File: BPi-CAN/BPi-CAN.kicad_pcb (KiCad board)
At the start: 2 copper layers, 100 x 100 mm, 124 parts, among them J1 RJ45, J2 RJ45, J3 RJ45, J4 RJ45, P1 BPi, P10 SPI, P11 SNIFFER, P12 CAN-Bus, P13 USB, P14 CAN-Bus, P15 POWER, P16 CAN, P17 CAN, P18 CAN, P19 TERM, P2 S88, P20 S88 CONN, P21 RS232 Con, P22 S88, P23 CONN_01X08, P24 CONN_01X03, P25 I2C-Bus, P26 CONN_01X02, P3 CONN_02X04, P4 BPi Con, P5 TERM, P6 S88, P7 I2C-Bus, P8 RS485, P9 RS232, U1 MCP2562, U10 MCP2562, U11 6N137, U12 ISO1050, U13 FT230XS, U2 LM7805, U3 6N137, U4 6N137, U5 6N137, U6 6N137, U7 ADuM1251BR, U8 MAX3072E, U9 MAX3232

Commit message: wip
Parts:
- added P27: POWER, Pin_Headers:Pin_Header_Straight_1x02, F.Cu at (147.4, 124.0)
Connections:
- P14 pad 3: /CB6 -> /CB6'
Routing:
- net /CB6: track 57.2 -> 48.9 mm, vias 5 -> 4
- net /CB6': track 0.00 -> 6.09 mm
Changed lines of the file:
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@@
-(kicad_pcb (version 4) (host pcbnew 4.0.1-stable)
+(kicad_pcb (version 4) (host pcbnew 4.0.2+dfsg1-stable)
   (general
-    (links 284)
+    (links 285)
     (no_connects 0)
-    (area 99.924999 39.924999 200.075001 140.075001)
+    (area 86.872087 28.15 207.5 148.200001)
     (thickness 1.6)
     (drawings 107)
     (tracks 1798)
     (zones 0)
-    (modules 124)
-    (nets 133)
+    (modules 125)
+    (nets 134)
   )
   (page A4)
@@
   (net 131 "Net-(P1-Pad2)")
   (net 132 "Net-(P1-Pad4)")
+  (net 133 /CB6')
   (net_class Default "This is the default net class."
     (clearance 0.2)
@@
     (uvia_drill 0.1)
     (add_net /CB6)
+    (add_net /CB6')
     (add_net "Net-(P15-Pad2)")
     (add_net "Net-(P23-Pad1)")
@@
       (effects (font (size 1.5 1.5) (thickness 0.3)))
     )
-    (fp_text value CAN-Bus (at 4.1402 -8.9662 90) (layer F.SilkS)
+    (fp_text value CAN-Bus (at 6.883 -9.341 90) (layer F.SilkS)
       (effects (font (size 1.5 1.5) (thickness 0.3)))
     )
@@
       (net 56 /CVCC))
     (pad 3 thru_hole circle (at 0 -0.7 90) (size 2.4 2.4) (drill 1.2) (layers *.Cu *.Mask F.SilkS)
-      (net 53 /CB6))
+      (net 133 /CB6'))
     (pad 4 thru_hole circle (at -3.5 -0.7 90) (size 2.4 2.4) (drill 1.2) (layers *.Cu *.Mask F.SilkS)
       (net 54 /CB7))
@@
     )
   )
+  (module Pin_Headers:Pin_Header_Straight_1x02 (layer F.Cu)
+    (at 147.4 124 90)
+    (descr "Through hole pin header")
+    (tags "pin header")
+    (fp_text reference P27 (at 0 -5.1 90) (layer F.SilkS)
+      (effects (font (size 1 1) (thickness 0.15)))
+    )
+    (fp_text value POWER (at 0 -3.1 90) (layer F.Fab)
+      (effects (font (size 1 1) (thickness 0.15)))
+    )
+    (fp_line (start 1.27 1.27) (end 1.27 3.81) (layer F.SilkS) (width 0.15))
+    (fp_line (start 1.55 -1.55) (end 1.55 0) (layer F.SilkS) (width 0.15))
+    (fp_line (start -1.75 -1.75) (end -1.75 4.3) (layer F.CrtYd) (width 0.05))
+    (fp_line (start 1.75 -1.75) (end 1.75 4.3) (layer F.CrtYd) (width 0.05))
+    (fp_line (start -1.75 -1.75) (end 1.75 -1.75) (layer F.CrtYd) (width 0.05))
+    (fp_line (start -1.75 4.3) (end 1.75 4.3) (layer F.CrtYd) (width 0.05))
+    (fp_line (start 1.27 1.27) (end -1.27 1.27) (layer F.SilkS) (width 0.15))
+    (fp_line (start -1.55 0) (end -1.55 -1.55) (layer F.SilkS) (width 0.15))
+    (fp_line (start -1.55 -1.55) (end 1.55 -1.55) (layer F.SilkS) (width 0.15))
+    (fp_line (start -1.27 1.27) (end -1.27 3.81) (layer F.SilkS) (width 0.15))
+    (fp_line (start -1.27 3.81) (end 1.27 3.81) (layer F.SilkS) (width 0.15))
+    (pad 1 thru_hole rect (at 0 0 90) (size 2.032 2.032) (drill 1.016) (layers *.Cu *.Mask F.SilkS)
+      (net 53 /CB6))
+    (pad 2 thru_hole oval (at 0 2.54 90) (size 2.032 2.032) (drill 1.016) (layers *.Cu *.Mask F.SilkS)
+      (net 133 /CB6'))
+    (model Pin_Headers.3dshapes/Pin_Header_Straight_1x02.wrl
+      (at (xyz 0 -0.05 0))
+      (scale (xyz 1 1 1))
+      (rotate (xyz 0 0 90))
+    )
+  )
   (gr_text RxD (at 105.41 70.6755 90) (layer F.SilkS)
     (effects (font (size 1.5 1.5) (thickness 0.3)))
@@
     (effects (font (size 0.8 0.8) (thickness 0.2)))
   )
-  (gr_text 5V (at 151.7904 124.6378) (layer F.SilkS)
+  (gr_text 5V (at 151.95 124.65) (layer F.SilkS)
     (effects (font (size 0.8 0.8) (thickness 0.2)))
   )
@@
   (segment (start 120.535 135.521) (end 120.535 130.46) (width 0.3048) (layer B.Cu) (net 52))
   (segment (start 141.635 130.46) (end 141.635 134.0185) (width 0.3048) (layer F.Cu) (net 52))
+  (segment (start 142.905 127.92) (end 142.905 127.895) (width 1.2) (layer B.Cu) (net 53))
+  (segment (start 142.905 127.895) (end 146.8 124) (width 1.2) (layer B.Cu) (net 53))
+  (segment (start 146.8 124) (end 147.4 124) (width 1.2) (layer B.Cu) (net 53))
   (segment (start 142.905 127.92) (end 142.905 127.4364) (width 1.2) (layer F.Cu) (net 53))
   (segment (start 142.905 127.4364) (end 141.5542 126.0856) (width 1.2) (layer F.Cu) (net 53))
@@
   (segment (start 121.805 124.8798) (end 122.6566 124.0282) (width 1.2) (layer B.Cu) (net 53))
   (segment (start 142.905 127.92) (end 142.905 127.8336) (width 1.2) (layer B.Cu) (net 53))
-  (segment (start 142.905 127.8336) (end 144.6784 126.0602) (width 1.2) (layer B.Cu) (net 53))
-  (segment (start 152.5016 124.333) (end 155.891 124.333) (width 1.2) (layer F.Cu) (net 53))
-  (segment (start 150.7744 126.0602) (end 152.5016 124.333) (width 1.2) (layer F.Cu) (net 53))
-  (via (at 150.7744 126.0602) (size 1.6) (layers F.Cu B.Cu) (net 53))
-  (segment (start 144.6784 126.0602) (end 150.7744 126.0602) (width 1.2) (layer B.Cu) (net 53))
   (segment (start 125.3998 110.6424) (end 125.3998 113.1824) (width 1.2) (layer B.Cu) (net 53))
   (segment (start 142.875 127.89) (end 142.905 127.92) (width 0.3048) (layer B.Cu) (net 53))
@@
   (segment (start 102.600101 59.400421) (end 102.529621 59.470901) (width 0.3048) (layer B.Cu) (net 130))
   (segment (start 102.600101 59.197899) (end 102.600101 59.400421) (width 0.3048) (layer B.Cu) (net 130))
+  (segment (start 149.94 124) (end 155.558 124) (width 1.2) (layer F.Cu) (net 133))
+  (segment (start 155.558 124) (end 155.891 124.333) (width 1.2) (layer F.Cu) (net 133))
   (zone (net 22) (net_name GNDD) (layer F.Cu) (hatch edge 0.508)
     (connect_pads (clearance 0.254))

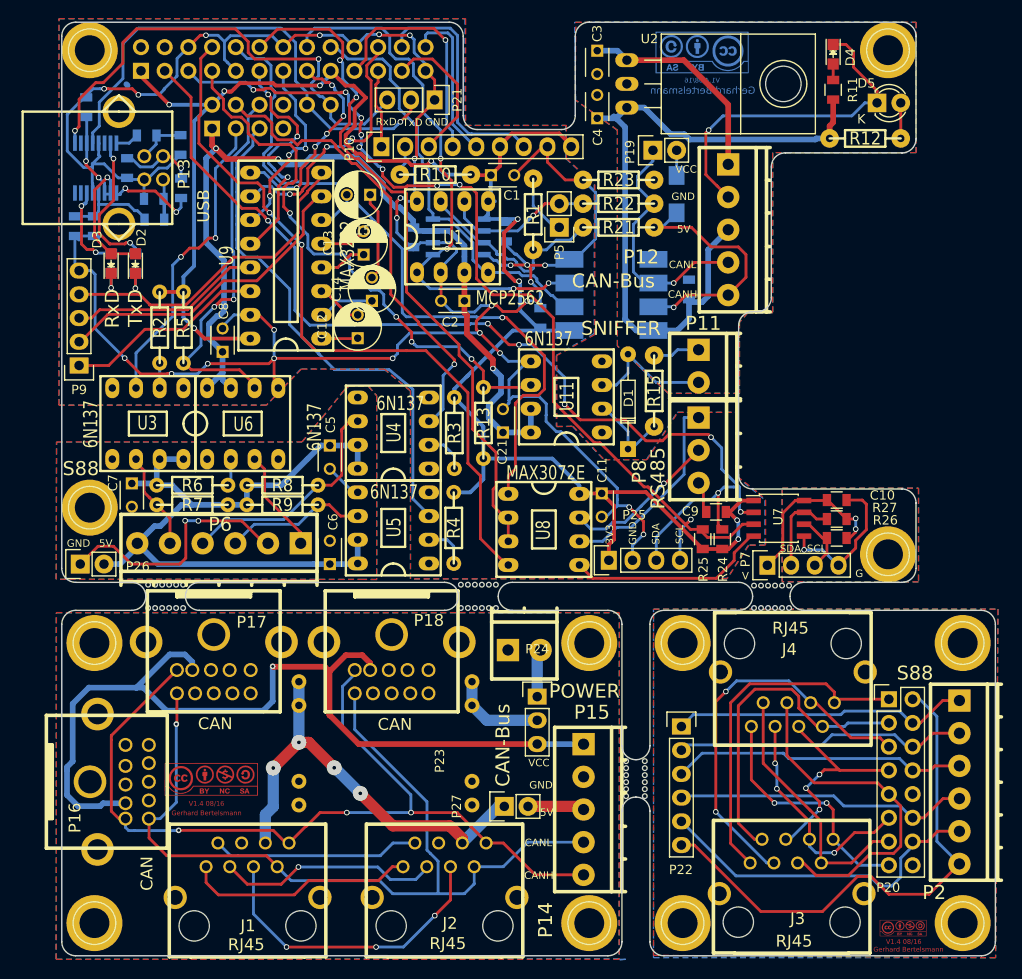
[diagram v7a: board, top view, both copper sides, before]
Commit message: add an new Jumper for M*rklin CAN adaptor board
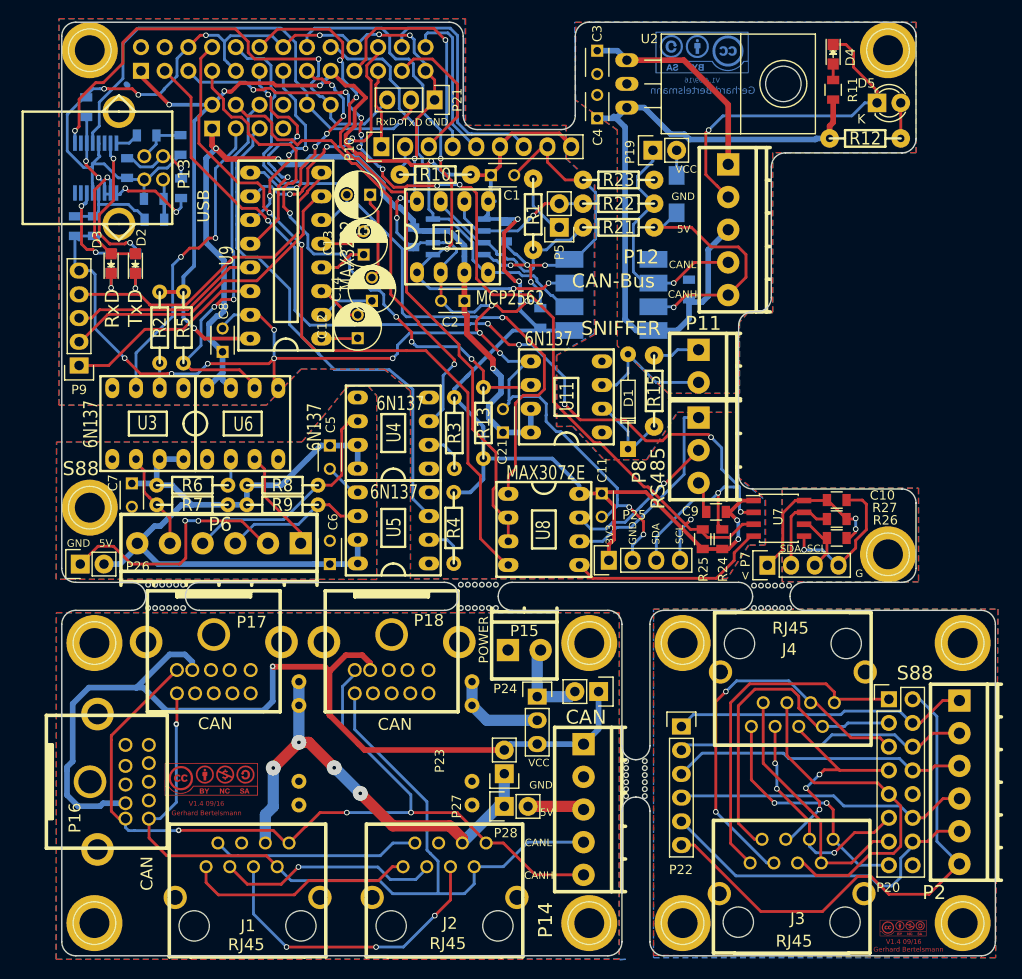
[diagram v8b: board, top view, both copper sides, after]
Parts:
- added P28: POWER, Pin_Headers:Pin_Header_Straight_1x02, F.Cu at (147.4, 120.5)
- added P29: POWER, Pin_Headers:Pin_Header_Straight_1x02, F.Cu at (157.5, 111.7)
- P14: value CAN-Bus -> CAN
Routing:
- net /CVCC: track 98.6 -> 105.5 mm
- net Net-(P15-Pad2): track 5.14 -> 9.40 mm
- net /CB6: track 48.9 -> 52.4 mm
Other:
- board text added: "V1.4 09/16"
- board text removed: "V1.4 08/16"
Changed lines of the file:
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@@
 (kicad_pcb (version 4) (host pcbnew 4.0.2+dfsg1-stable)
   (general
-    (links 285)
+    (links 289)
     (no_connects 0)
     (area 86.872087 28.15 207.5 148.200001)
     (thickness 1.6)
     (drawings 107)
-    (tracks 1798)
+    (tracks 1806)
     (zones 0)
-    (modules 125)
+    (modules 127)
     (nets 134)
   )
@@
     (at 149.5425 106.553 180)
     (descr "2-way 3.5mm pitch terminal block, Phoenix PT series")
-    (fp_text reference P15 (at -7.239 -7.366 180) (layer F.SilkS)
-      (effects (font (size 1.5 1.5) (thickness 0.3)))
+    (fp_text reference P15 (at -0.0075 1.353 180) (layer F.SilkS)
+      (effects (font (size 1.2 1.2) (thickness 0.3)))
     )
-    (fp_text value POWER (at -6.4389 -5.1054 180) (layer F.SilkS)
-      (effects (font (size 1.5 1.5) (thickness 0.3)))
+    (fp_text value POWER (at 4.3425 0.403 270) (layer F.SilkS)
+      (effects (font (size 1 1) (thickness 0.25)))
     )
     (fp_line (start 0 3.4) (end 0 3.8) (layer F.SilkS) (width 0.381))
@@
       (effects (font (size 1.5 1.5) (thickness 0.3)))
     )
-    (fp_text value CAN-Bus (at 6.883 -9.341 90) (layer F.SilkS)
+    (fp_text value CAN (at 9.883 -0.441 180) (layer F.SilkS)
       (effects (font (size 1.5 1.5) (thickness 0.3)))
     )
@@
     (descr "Through hole pin header")
     (tags "pin header")
-    (fp_text reference P24 (at 0 -5.1) (layer F.SilkS)
+    (fp_text reference P24 (at -3.4268 -0.8426) (layer F.SilkS)
       (effects (font (size 1 1) (thickness 0.15)))
     )
@@
       (effects (font (size 1 1) (thickness 0.15)))
     )
-    (fp_text value LED (at -3.2385 0 90) (layer F.Fab)
+    (fp_text value LED (at -3.2385 0 90) (layer F.Fab) hide
       (effects (font (size 1 1) (thickness 0.15)))
     )
@@
       (effects (font (size 1 1) (thickness 0.15)))
     )
-    (fp_text value LED (at -3.2385 0.0635 90) (layer F.Fab)
+    (fp_text value LED (at -3.2385 0.0635 90) (layer F.Fab) hide
       (effects (font (size 1 1) (thickness 0.15)))
     )
@@
       (effects (font (size 1 1) (thickness 0.15)))
     )
-    (fp_text value POWER (at 0 -3.1 90) (layer F.Fab)
+    (fp_text value POWER (at 0 -3.1 90) (layer F.Fab) hide
       (effects (font (size 1 1) (thickness 0.15)))
     )
@@
     )
   )
+  (module Pin_Headers:Pin_Header_Straight_1x02 (layer F.Cu)
+    (at 147.4 120.5 180)
+    (descr "Through hole pin header")
+    (tags "pin header")
+    (fp_text reference P28 (at -0.15 -6.35 180) (layer F.SilkS)
+      (effects (font (size 1 1) (thickness 0.15)))
+    )
+    (fp_text value POWER (at 0 -3.1 180) (layer F.Fab) hide
+      (effects (font (size 1 1) (thickness 0.15)))
+    )
+    (fp_line (start 1.27 1.27) (end 1.27 3.81) (layer F.SilkS) (width 0.15))
+    (fp_line (start 1.55 -1.55) (end 1.55 0) (layer F.SilkS) (width 0.15))
+    (fp_line (start -1.75 -1.75) (end -1.75 4.3) (layer F.CrtYd) (width 0.05))
+    (fp_line (start 1.75 -1.75) (end 1.75 4.3) (layer F.CrtYd) (width 0.05))
+    (fp_line (start -1.75 -1.75) (end 1.75 -1.75) (layer F.CrtYd) (width 0.05))
+    (fp_line (start -1.75 4.3) (end 1.75 4.3) (layer F.CrtYd) (width 0.05))
+    (fp_line (start 1.27 1.27) (end -1.27 1.27) (layer F.SilkS) (width 0.15))
+    (fp_line (start -1.55 0) (end -1.55 -1.55) (layer F.SilkS) (width 0.15))
+    (fp_line (start -1.55 -1.55) (end 1.55 -1.55) (layer F.SilkS) (width 0.15))
+    (fp_line (start -1.27 1.27) (end -1.27 3.81) (layer F.SilkS) (width 0.15))
+    (fp_line (start -1.27 3.81) (end 1.27 3.81) (layer F.SilkS) (width 0.15))
+    (pad 1 thru_hole rect (at 0 0 180) (size 2.032 2.032) (drill 1.016) (layers *.Cu *.Mask F.SilkS)
+      (net 53 /CB6))
+    (pad 2 thru_hole oval (at 0 2.54 180) (size 2.032 2.032) (drill 1.016) (layers *.Cu *.Mask F.SilkS)
+      (net 56 /CVCC))
+    (model Pin_Headers.3dshapes/Pin_Header_Straight_1x02.wrl
+      (at (xyz 0 -0.05 0))
+      (scale (xyz 1 1 1))
+      (rotate (xyz 0 0 90))
+    )
+  )
+  (module Pin_Headers:Pin_Header_Straight_1x02 (layer F.Cu)
+    (at 157.5 111.7 270)
+    (descr "Through hole pin header")
+    (tags "pin header")
+    (fp_text reference P29 (at -0.05 -3.25 270) (layer F.SilkS) hide
+      (effects (font (size 1 1) (thickness 0.15)))
+    )
+    (fp_text value POWER (at 0.1 -3.25 270) (layer F.Fab)
+      (effects (font (size 1 1) (thickness 0.15)))
+    )
+    (fp_line (start 1.27 1.27) (end 1.27 3.81) (layer F.SilkS) (width 0.15))
+    (fp_line (start 1.55 -1.55) (end 1.55 0) (layer F.SilkS) (width 0.15))
+    (fp_line (start -1.75 -1.75) (end -1.75 4.3) (layer F.CrtYd) (width 0.05))
+    (fp_line (start 1.75 -1.75) (end 1.75 4.3) (layer F.CrtYd) (width 0.05))
+    (fp_line (start -1.75 -1.75) (end 1.75 -1.75) (layer F.CrtYd) (width 0.05))
+    (fp_line (start -1.75 4.3) (end 1.75 4.3) (layer F.CrtYd) (width 0.05))
+    (fp_line (start 1.27 1.27) (end -1.27 1.27) (layer F.SilkS) (width 0.15))
+    (fp_line (start -1.55 0) (end -1.55 -1.55) (layer F.SilkS) (width 0.15))
+    (fp_line (start -1.55 -1.55) (end 1.55 -1.55) (layer F.SilkS) (width 0.15))
+    (fp_line (start -1.27 1.27) (end -1.27 3.81) (layer F.SilkS) (width 0.15))
+    (fp_line (start -1.27 3.81) (end 1.27 3.81) (layer F.SilkS) (width 0.15))
+    (pad 1 thru_hole rect (at 0 0 270) (size 2.032 2.032) (drill 1.016) (layers *.Cu *.Mask F.SilkS)
+      (net 56 /CVCC))
+    (pad 2 thru_hole oval (at 0 2.54 270) (size 2.032 2.032) (drill 1.016) (layers *.Cu *.Mask F.SilkS)
+      (net 122 "Net-(P15-Pad2)"))
+    (model Pin_Headers.3dshapes/Pin_Header_Straight_1x02.wrl
+      (at (xyz 0 -0.05 0))
+      (scale (xyz 1 1 1))
+      (rotate (xyz 0 0 90))
+    )
+  )
   (gr_text RxD (at 105.41 70.6755 90) (layer F.SilkS)
     (effects (font (size 1.5 1.5) (thickness 0.3)))
@@
     (effects (font (size 1.5 1.5) (thickness 0.3)))
   )
-  (gr_text "V1.4 08/16" (at 168.5925 46.228) (layer B.Cu)
+  (gr_text "V1.4 09/16" (at 168.5925 46.228) (layer B.Cu)
     (effects (font (size 0.508 0.508) (thickness 0.127)) (justify mirror))
   )
@@
     (effects (font (size 0.508 0.508) (thickness 0.0635)))
   )
-  (gr_text "V1.4 08/16" (at 115.5065 123.698) (layer F.Cu)
+  (gr_text "V1.4 09/16" (at 115.5065 123.698) (layer F.Cu)
     (effects (font (size 0.508 0.508) (thickness 0.127)))
   )
-  (gr_text "V1.4 08/16" (at 190.1825 138.4935) (layer F.Cu)
+  (gr_text "V1.4 09/16" (at 190.1825 138.4935) (layer F.Cu)
     (effects (font (size 0.508 0.508) (thickness 0.127)))
   )
@@
   (segment (start 120.535 135.521) (end 120.535 130.46) (width 0.3048) (layer B.Cu) (net 52))
   (segment (start 141.635 130.46) (end 141.635 134.0185) (width 0.3048) (layer F.Cu) (net 52))
+  (segment (start 147.4 124) (end 147.4 120.5) (width 1.2) (layer B.Cu) (net 53))
   (segment (start 142.905 127.92) (end 142.905 127.895) (width 1.2) (layer B.Cu) (net 53))
   (segment (start 142.905 127.895) (end 146.8 124) (width 1.2) (layer B.Cu) (net 53))
@@
   (segment (start 126.2126 126.111) (end 126.154 126.111) (width 0.3048) (layer F.Cu) (net 55))
   (segment (start 126.154 126.111) (end 124.345 127.92) (width 0.3048) (layer F.Cu) (net 55))
+  (segment (start 157.5 111.7) (end 157.5 115.724) (width 0.6096) (layer B.Cu) (net 56))
+  (segment (start 157.5 115.724) (end 155.891 117.333) (width 0.6096) (layer B.Cu) (net 56))
+  (segment (start 147.4 117.96) (end 132.438 117.96) (width 0.6096) (layer F.Cu) (net 56))
+  (segment (start 131.8006 117.3226) (end 128.6764 114.1984) (width 0.6096) (layer F.Cu) (net 56))
+  (segment (start 132.438 117.96) (end 131.8006 117.3226) (width 0.6096) (layer F.Cu) (net 56))
+  (segment (start 150.9268 117.3226) (end 148.0374 117.3226) (width 0.6096) (layer B.Cu) (net 56))
+  (segment (start 148.0374 117.3226) (end 147.4 117.96) (width 0.6096) (layer B.Cu) (net 56))
   (segment (start 107.9754 111.2774) (end 108.7374 111.2774) (width 0.6096) (layer B.Cu) (net 56))
   (segment (start 122.5931 112.7379) (end 122.5931 109.0041) (width 0.6096) (layer B.Cu) (net 56))
@@
   (segment (start 113.9812 108.5202) (end 113.9812 109.3912) (width 0.6096) (layer B.Cu) (net 56))
   (segment (start 113.1824 107.7214) (end 113.9812 108.5202) (width 0.6096) (layer B.Cu) (net 56))
-  (segment (start 150.9268 117.3226) (end 131.8006 117.3226) (width 0.6096) (layer F.Cu) (net 56))
-  (segment (start 131.8006 117.3226) (end 128.6764 114.1984) (width 0.6096) (layer F.Cu) (net 56))
   (segment (start 133.0312 109.3912) (end 133.0312 108.6472) (width 0.6096) (layer F.Cu) (net 56))
   (segment (start 133.0312 108.6472) (end 132.1816 107.7976) (width 0.6096) (layer F.Cu) (net 56))
@@
   (segment (start 150.9268 114.7826) (end 145.542 114.7826) (width 1.2) (layer B.Cu) (net 121))
   (segment (start 145.542 114.7826) (end 143.9418 113.1824) (width 1.2) (layer B.Cu) (net 121))
+  (segment (start 150.9268 112.2426) (end 154.4174 112.2426) (width 1.2) (layer B.Cu) (net 122))
+  (segment (start 154.4174 112.2426) (end 154.96 111.7) (width 1.2) (layer B.Cu) (net 122))
   (segment (start 150.9268 112.2426) (end 150.9268 107.6187) (width 1.2) (layer B.Cu) (net 122))
   (segment (start 150.9268 107.6187) (end 151.2925 107.253) (width 1.2) (layer B.Cu) (net 122))
